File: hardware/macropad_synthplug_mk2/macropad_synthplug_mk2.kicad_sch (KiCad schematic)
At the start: 38 parts, among them J1 Qwiic_RA, J2 AudioJack4, J3 AudioJack4, J4 AudioJack4, J5 Conn_01x04, SW1 K3-2346S-L1, SW2 K3-2346S-L1, U1 H11L1S(TA), U2 74HC14

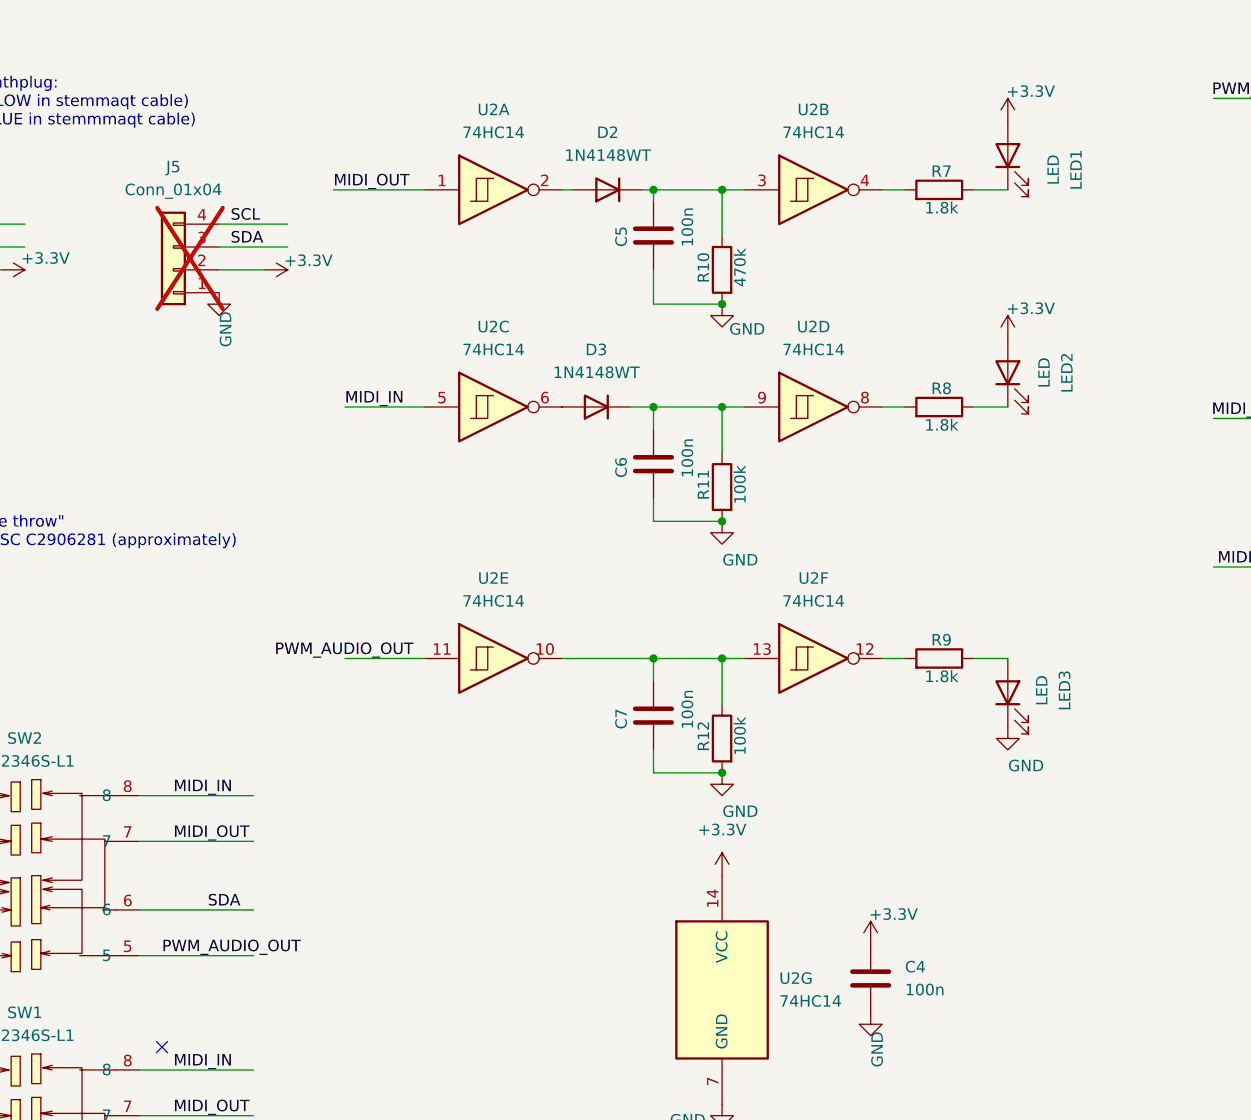
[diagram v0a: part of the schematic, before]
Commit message: mk2 size and silkscreen update
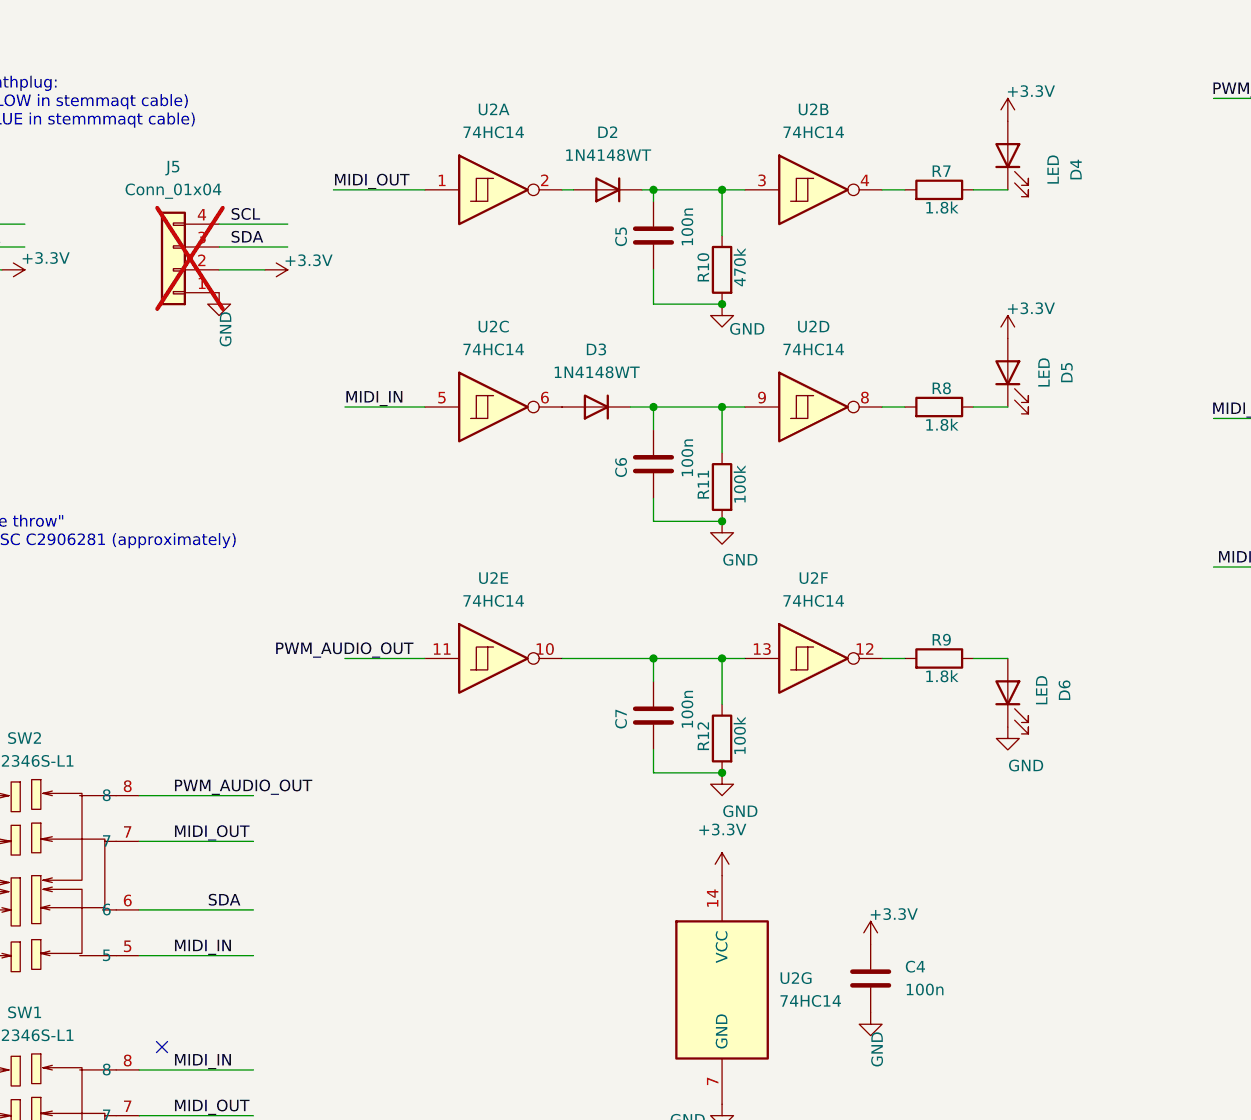
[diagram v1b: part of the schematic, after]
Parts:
- renumbered LED1 to D4, LED2 to D5, LED3 to D6
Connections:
- net MIDI_IN: now also SW2.5; no longer SW2.8
- net PWM_AUDIO_OUT: now also SW2.8; no longer SW2.5
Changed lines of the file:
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@@
 	(wire
 		(pts
+			(xy 60.96 102.87) (xy 73.66 102.87)
+		)
+		(stroke
+			(width 0)
+			(type default)
+		)
+	)
+	(wire
+		(pts
 			(xy 143.51 59.69) (xy 146.05 59.69)
 		)
@@
 	(wire
 		(pts
-			(xy 60.96 102.87) (xy 73.66 102.87)
-		)
-		(stroke
-			(width 0)
-			(type default)
-		)
-	)
-	(wire
-		(pts
 			(xy 180.34 77.47) (xy 238.76 77.47)
 		)
@@
 	)
 	(label "MIDI_IN"
-		(at 64.77 102.87 0)
+		(at 64.77 120.65 0)
 		(fields_autoplaced yes)
 		(effects
@@
 	)
 	(label "PWM_AUDIO_OUT"
-		(at 63.5 120.65 0)
+		(at 64.77 102.87 0)
 		(fields_autoplaced yes)
 		(effects
@@
 		(on_board yes)
 		(dnp no)
-		(property "Reference" "LED1"
+		(property "Reference" "D4"
 			(at 165.1 33.3375 0)
 			(effects
@@
 			(project ""
 				(path "/5e6a2468-e052-4e22-bfa1-3eaff724ccf3"
-					(reference "LED1")
+					(reference "D4")
 					(unit 1)
 				)
@@
 		(on_board yes)
 		(dnp no)
-		(property "Reference" "LED3"
+		(property "Reference" "D6"
 			(at 163.83 91.186 0)
 			(effects
@@
 			(project "macropad_synthplug_mk2"
 				(path "/5e6a2468-e052-4e22-bfa1-3eaff724ccf3"
-					(reference "LED3")
+					(reference "D6")
 					(unit 1)
 				)
@@
 		(on_board yes)
 		(dnp no)
-		(property "Reference" "LED2"
+		(property "Reference" "D5"
 			(at 164.084 55.88 0)
 			(effects
@@
 			(project "macropad_synthplug_mk2"
 				(path "/5e6a2468-e052-4e22-bfa1-3eaff724ccf3"
-					(reference "LED2")
+					(reference "D5")
 					(unit 1)
 				)
